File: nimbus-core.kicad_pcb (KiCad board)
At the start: 4 copper layers, 61.9 x 61.9 mm, 59 parts, among them J1 Val**, J2 Val**, J3 532614006, J4 USB4105-GF-A-120, J5 532614006, U1 LQFP100, U3 SOIC-8, U5 SOT-666-6, Y1 25MHz

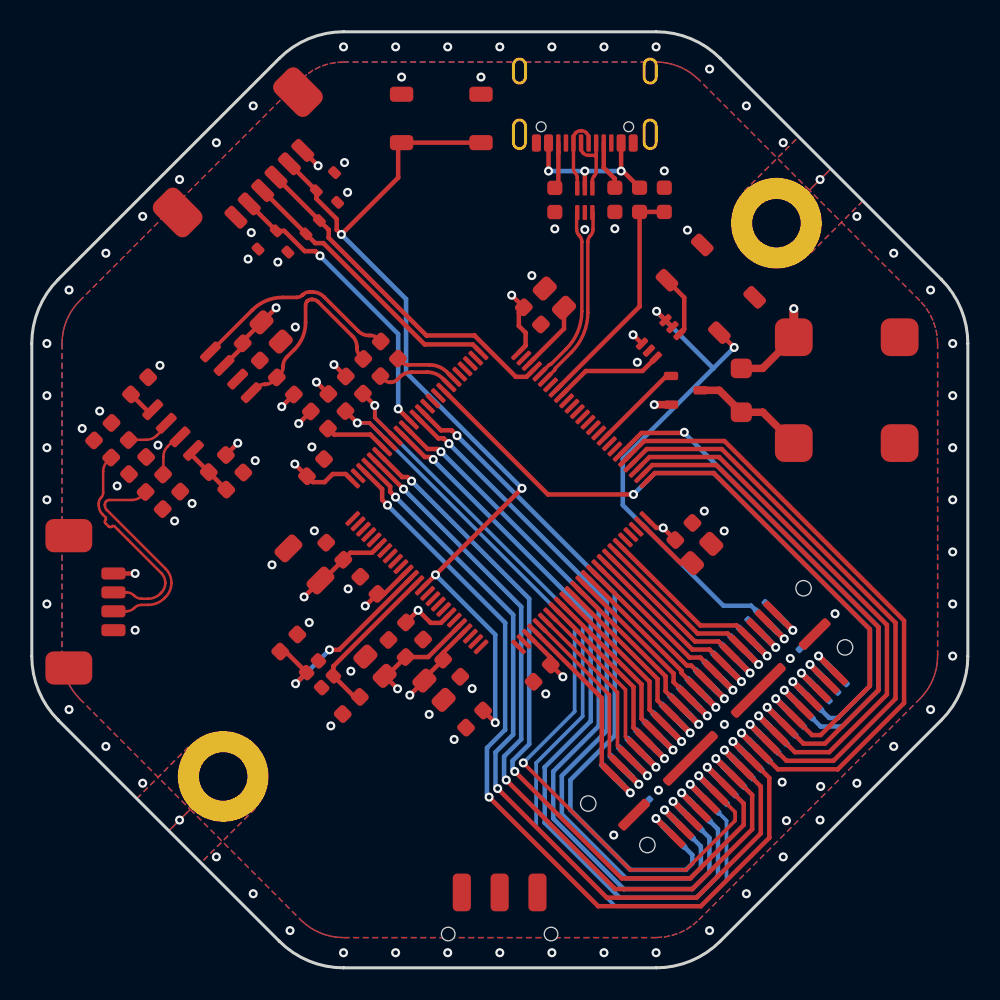
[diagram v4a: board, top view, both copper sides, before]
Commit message: Improve CAN driver layout to be more compact
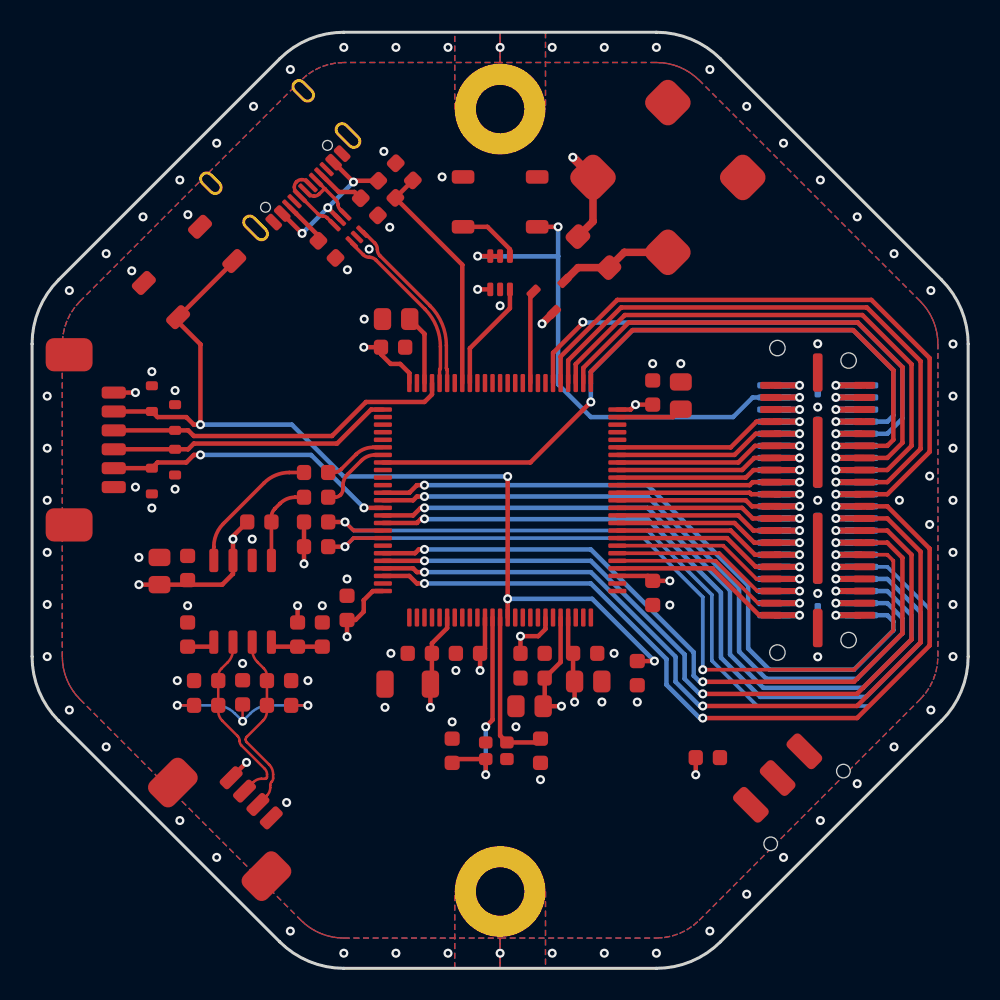
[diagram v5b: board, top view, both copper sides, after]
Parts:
- moved R1 34.0 mm to (164.0, 121.4), turned to 180 degrees
- moved SW2 22.0 mm to (170.6, 124.7), turned to 45 degrees
- moved J5 21.5 mm to (122.5, 100.4), turned to 90 degrees
- moved REF** 19.8 mm to (150.3, 130.3), turned to 0 degrees
- moved REF** 19.8 mm to (150.3, 78.5), turned to 180 degrees
- moved SW1 19.5 mm to (129.7, 89.3), turned to 45 degrees
- moved J4 19.0 mm to (137.2, 83.3), turned to -135 degrees
- moved U2 18.4 mm to (161.4, 83.0), turned to 45 degrees
- moved D2 18.4 mm to (127.3, 97.7), turned to 90 degrees
- moved R9 18.3 mm to (130.9, 117.9), turned to 0 degrees
- moved D5 17.7 mm to (127.3, 103.1), turned to -90 degrees
- moved J3 17.6 mm to (132.2, 125.7), turned to 135 degrees
- moved C12 17.4 mm to (127.8, 109.1), turned to 90 degrees
- moved C20 17.4 mm to (130.9, 116.3), turned to 180 degrees
- moved R13 17.3 mm to (144.0, 82.7), turned to -45 degrees
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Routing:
- net Net-(C22-Pad1): track 0.00 -> 12.7 mm
- net Net-(U3-TXD): track 13.4 -> 5.65 mm
- net /CAN_N: track 17.6 -> 12.3 mm
- net /CAN_P: track 17.7 -> 12.6 mm
- net +3.3V: track 69.7 -> 74.5 mm, vias 21 -> 20
- net Net-(U3-RXD): track 13.9 -> 9.21 mm
- net /BOOT0: track 4.32 -> 0.00 mm
- net GND: vias 42 -> 43

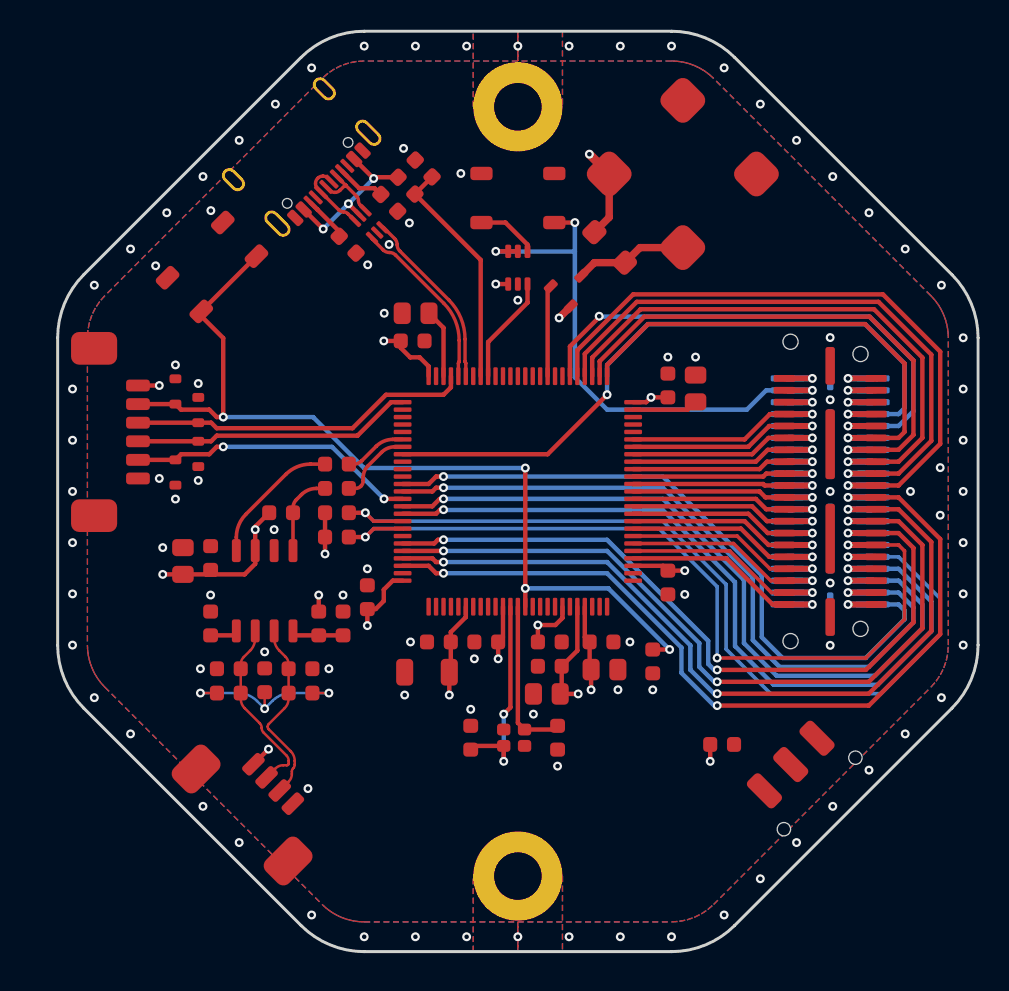
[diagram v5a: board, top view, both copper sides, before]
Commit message: Position BOOT0 SPDT switch, refill zones and add stitching vias for GND
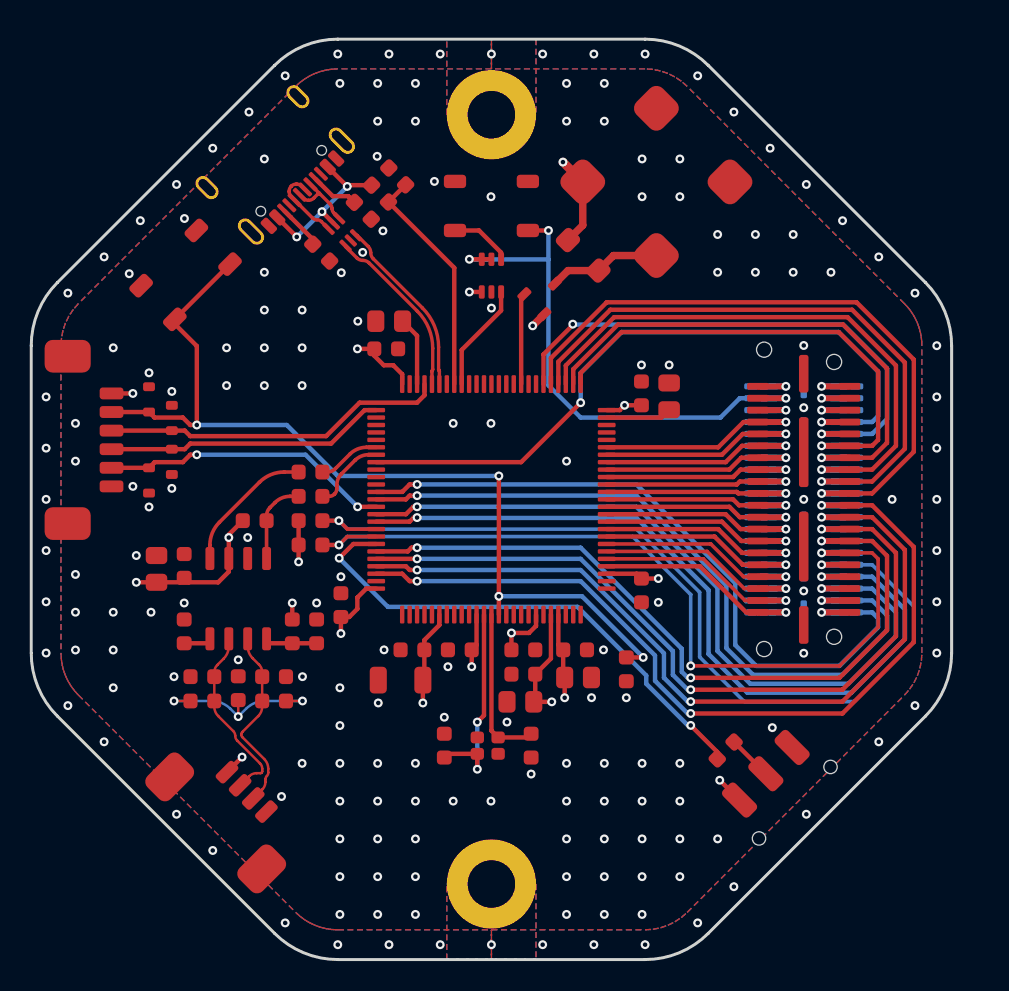
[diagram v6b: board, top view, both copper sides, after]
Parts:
- moved C1 1.86 mm to (157.6, 116.4)
- moved C16 1.86 mm to (141.5, 94.8)
- moved C19 1.86 mm to (142.4, 117.1)
- moved C21 1.86 mm to (133.9, 116.8)
- moved R5 1.86 mm to (135.1, 113.8)
- moved U5 1.86 mm to (138.5, 86.9)
- moved R15 1.86 mm to (137.1, 88.3)
- moved C17 1.86 mm to (138.4, 112.0)
- moved C7 1.86 mm to (154.2, 115.0)
- moved C8 1.86 mm to (160.5, 98.0)
- moved R7 1.86 mm to (136.8, 113.8)
- moved C15 1.86 mm to (127.9, 109.4)
- moved Q1 1.86 mm to (152.1, 91.1)
- moved R10 1.86 mm to (136.4, 106.4)
- moved C13 1.86 mm to (158.6, 97.8)
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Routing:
- net /BOOT0: track 0.00 -> 34.5 mm, vias 0 -> 2
- net Net-(R1-Pad2): track 1.13 -> 3.02 mm, vias 1 -> 0
- net +3.3V: track 74.5 -> 76.3 mm
- net GND: vias 43 -> 127
- net CHASSIS: vias 53 -> 51

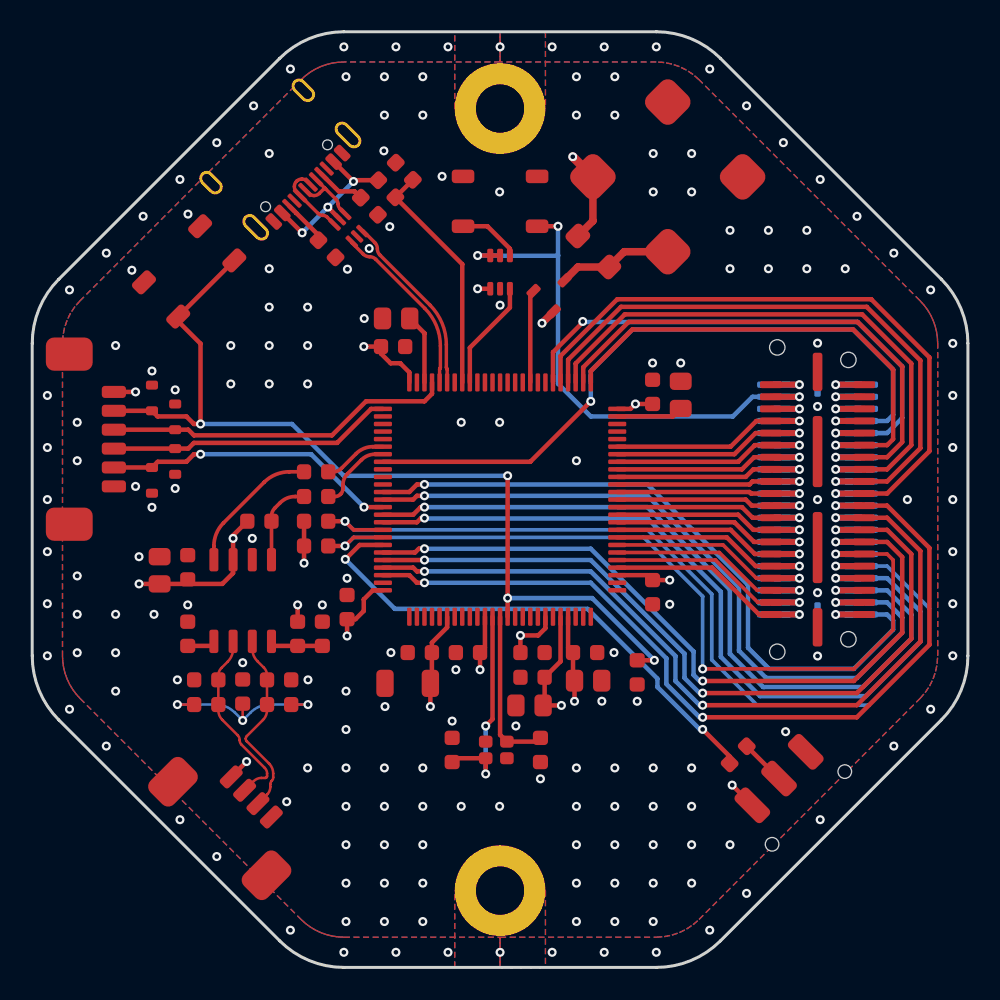
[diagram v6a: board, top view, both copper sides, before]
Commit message: Use new worksheet template
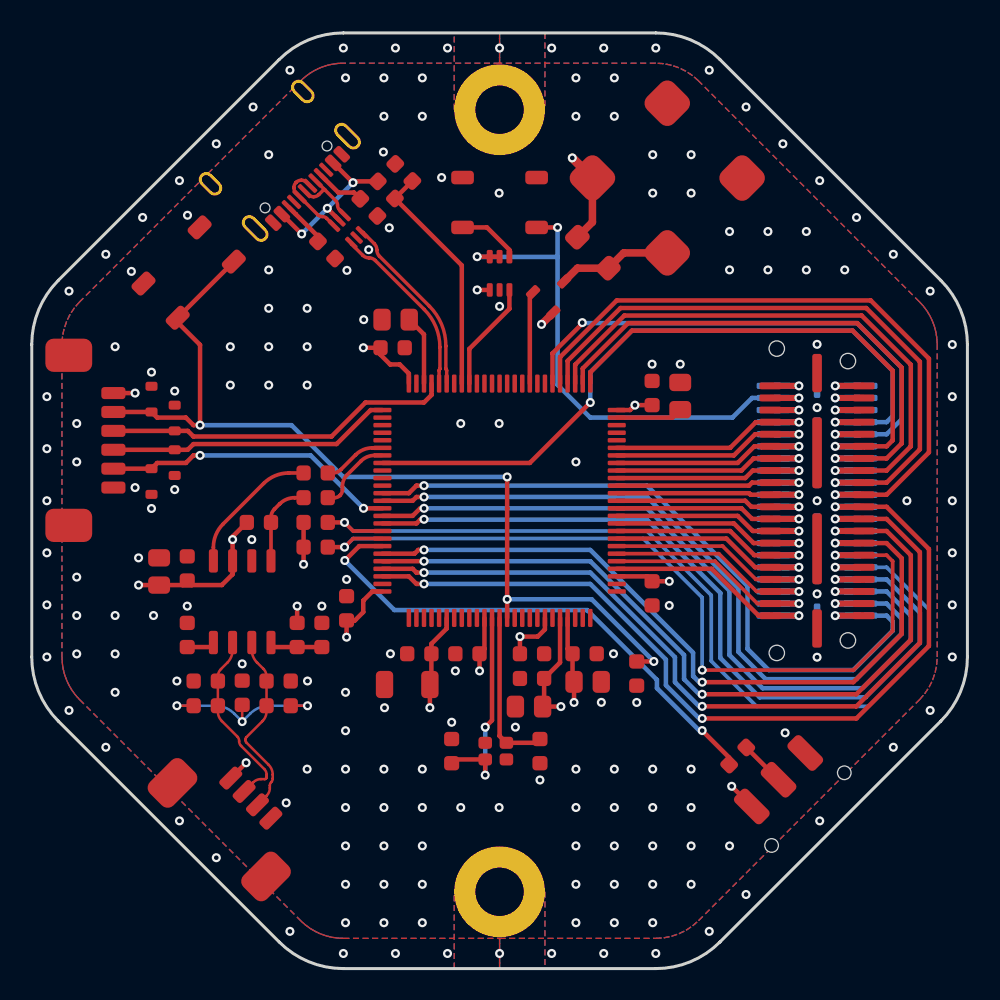
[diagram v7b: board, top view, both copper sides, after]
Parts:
- moved C10 0.08 mm to (154.3, 117.0)
- moved C18 0.08 mm to (143.2, 115.1)
- moved C6 0.08 mm to (150.6, 115.1)
- moved D1 0.08 mm to (154.7, 88.6)
- moved D3 0.08 mm to (127.0, 99.5)
- moved D4 0.08 mm to (127.0, 102.5)
- moved J3 0.08 mm to (130.4, 126.3)
- moved R10 0.08 mm to (136.3, 106.4)
- moved R4 0.08 mm to (132.6, 106.4)
- moved R9 0.08 mm to (129.1, 118.6)
- moved U2 0.08 mm to (159.6, 83.7)
- moved U6 0.08 mm to (148.5, 85.3)
- moved R15 0.08 mm to (137.1, 88.4)
- moved R8 0.08 mm to (133.9, 118.6)
- moved C1 0.08 mm to (157.6, 116.4)
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
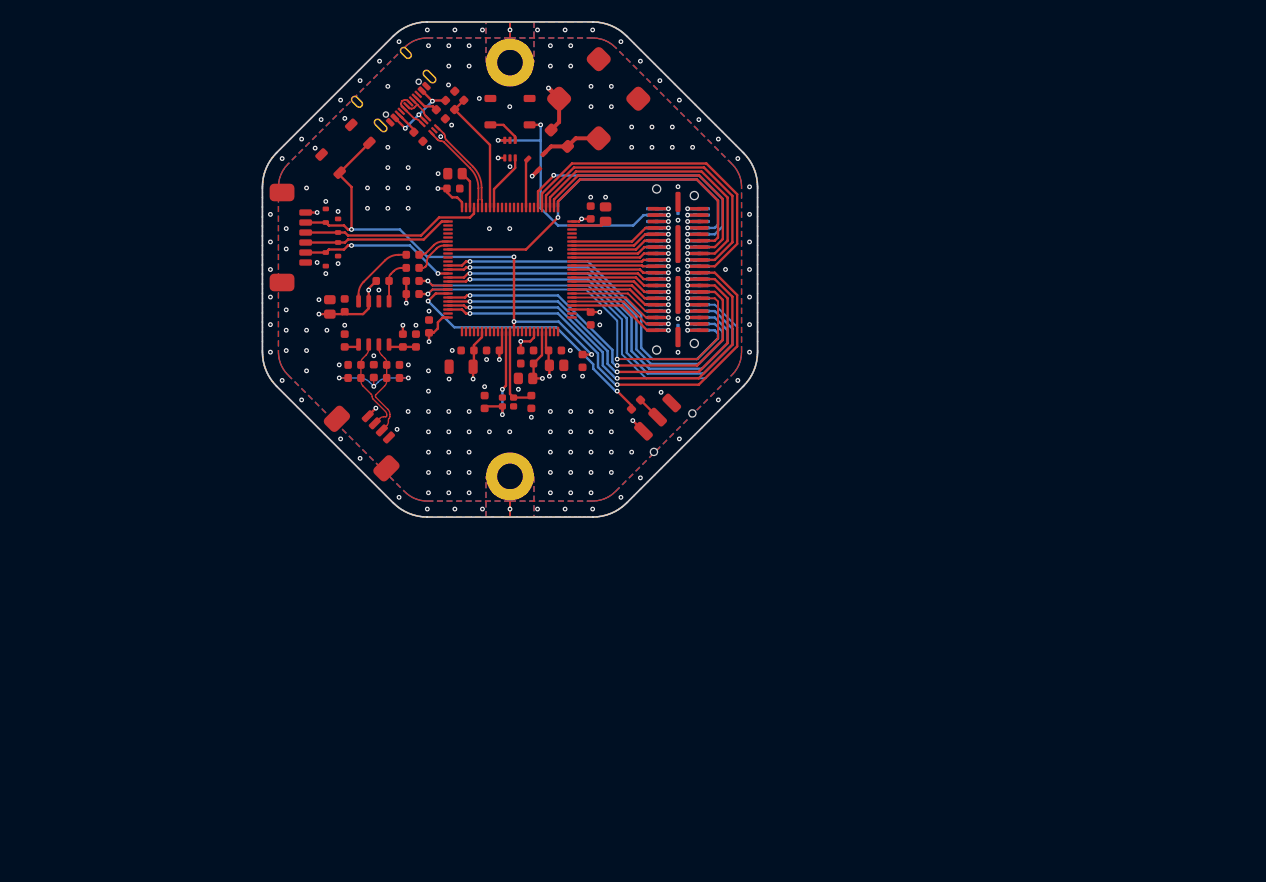
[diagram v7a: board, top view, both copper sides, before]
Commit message: Update worksheet template in PCB
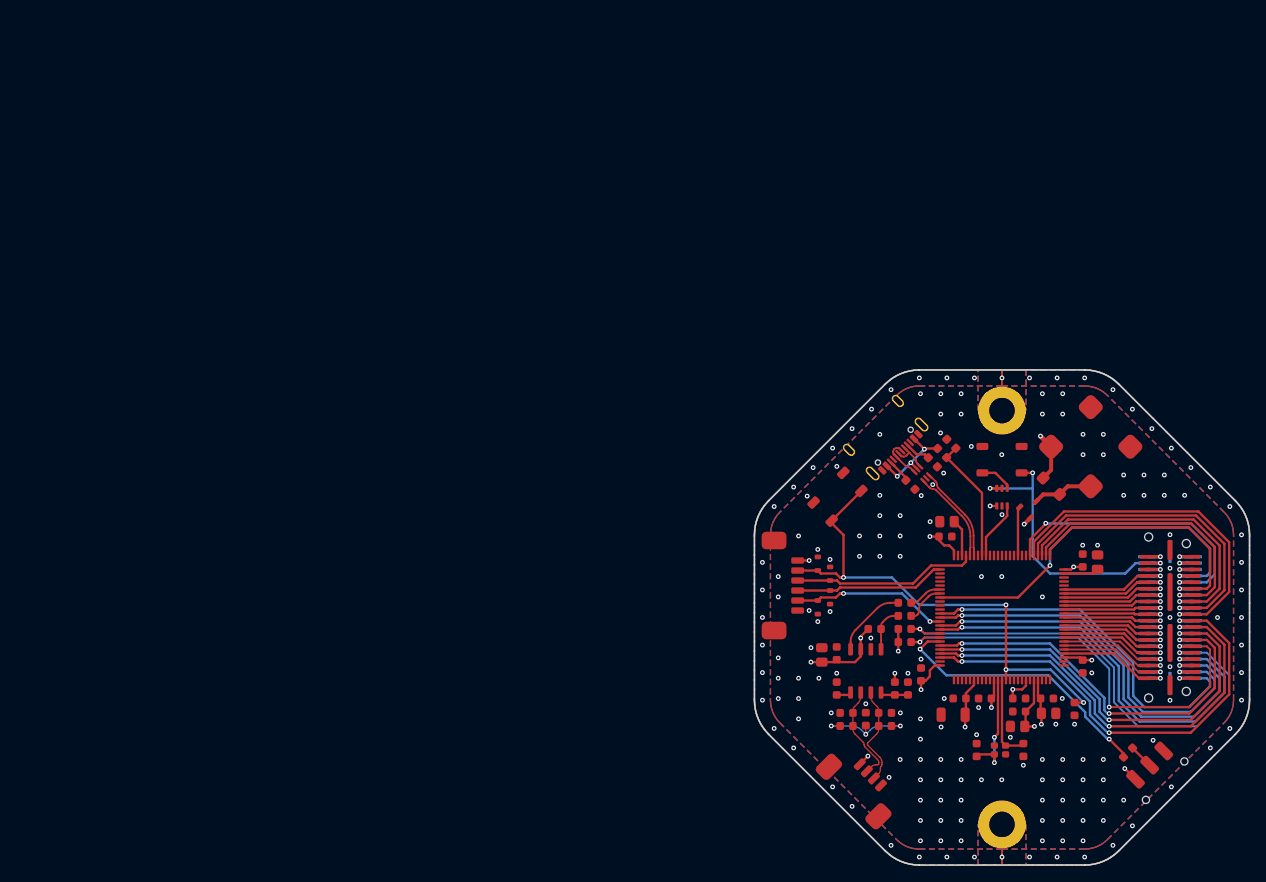
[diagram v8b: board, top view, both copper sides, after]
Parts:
- moved C12 75.3 mm to (187.5, 153.2)
- moved D3 75.3 mm to (188.5, 143.0)
- moved D4 75.3 mm to (188.5, 146.0)
- moved C1 75.3 mm to (219.1, 159.9)
- moved C11 75.3 mm to (212.1, 160.3)
- moved C13 75.3 mm to (220.1, 141.4)
- moved C14 75.3 mm to (211.9, 162.1)
- moved C15 75.3 mm to (189.3, 153.0)
- moved C17 75.3 mm to (199.9, 155.6)
- moved C18 75.3 mm to (204.7, 158.6)
- moved C19 75.3 mm to (203.9, 160.7)
- moved C2 75.3 mm to (206.8, 165.1)
- moved C20 75.3 mm to (190.6, 160.4)
- moved C21 75.3 mm to (195.4, 160.4)
- moved C22 75.3 mm to (193.0, 161.2)
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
